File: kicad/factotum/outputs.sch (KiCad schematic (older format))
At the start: 68 parts

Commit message: working on schematic
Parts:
- removed R? (x14): R_Small, symbol Device:R_Small
- added C29, C30: 100n, symbol Device:C_Small
- added J13: Conn_01x10_Female, symbol Connector:Conn_01x10_Female
- added J18: Conn_01x10_Male, symbol Connector:Conn_01x10_Male
- added J19: Conn_01x18_Female, symbol Connector:Conn_01x18_Female
- added J20: Conn_01x18_Male, symbol Connector:Conn_01x18_Male
- added R51: 10k, symbol Device:R_Small
- added R54, R56, R58, R60, R62, R64, R66: 68, symbol Device:R_Small
- added R55, R57, R59, R61, R63, R65, R67: 56, symbol Device:R_Small
- added unit 5 of U6
- added unit 5 of U7
- D10, D11, D4, D5, D6, D7, D8, D9: renamed from D?; value LED_Dual_CAC -> SSL-LX3059IGW-CA
- R52: renamed from R?; value R_Small -> 68
- R53: renamed from R?; value R_Small -> 56
- gave numbers to parts that had none: 38
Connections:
- net DAC0 is gone; now on net DAC1: U10.3 (VOUTA)
- net +3.3VA: now also C29.1, U6.11 (V-), U7.11 (V-)
- net +3V3: now also C30.1, J19.1 (Pin_1), J20.1 (Pin_1), R51.2
- net DAC1: no longer U10.4 (VOUTB)
- net DAC2: now also U10.4 (VOUTB); no longer U10.5 (VOUTC)
- net DAC3: now also U10.5 (VOUTC); no longer U10.6 (VOUTD)
- net DAC4: now also U10.6 (VOUTD); no longer U10.14 (VOUTE)
- net DAC5: now also U10.14 (VOUTE); no longer U10.13 (VOUTF)
- net DAC6: now also U10.13 (VOUTF); no longer U10.12 (VOUTG)
- net DAC7: now also U10.12 (VOUTG); no longer U10.11 (VOUTH)
- net DAC8: now also U10.11 (VOUTH)
- net GND: now also C29.2, C30.2, J13.10 (Pin_10), J18.10 (Pin_10), J19.18 (Pin_18), J20.18 (Pin_18), U6.4 (V+), U7.4 (V+)
- net VREF: now also U6.10 (+), U6.12 (+), U6.5 (+), U7.10 (+), U7.12 (+), U7.5 (+), J13.1 (Pin_1), J18.1 (Pin_1); no longer U6.3 (+), U6.3 (+), U6.3 (+), U7.3 (+), U7.3 (+), U7.3 (+)
- net B_2: now reaches R43.1, R48.1
- net B_2: now also J18.3 (Pin_3); no longer J14.S
- net B_1: now reaches R31.1, R35.1
- net B_1: now also J18.2 (Pin_2); no longer J9.S
- net at R49.2: now also U7.7; no longer U7.1
- net at R40.1, R44.2: now also U7.6 (-); no longer U7.2 (-)
- net B_4: now reaches R44.1, R49.1
- net B_4: now also J18.5 (Pin_5); no longer J15.S
- net at R36.2: now also U6.7; no longer U6.1
- net at R26.1, R32.2: now also U6.6 (-); no longer U6.2 (-)
- net B_3: now reaches R32.1, R36.1
- net B_3: now also J18.4 (Pin_4); no longer J10.S
- net at R50.2: now also U7.8; no longer U7.1
- net at R41.1, R45.2: now also U7.9 (-); no longer U7.2 (-)
- net B_6: now reaches R45.1, R50.1
- net B_6: now also J18.7 (Pin_7); no longer J16.S
- net at R37.2: now also U6.8; no longer U6.1
- net at R27.1, R33.2: now also U6.9 (-); no longer U6.2 (-)
- net B_5: now reaches R33.1, R37.1
- net B_5: now also J18.6 (Pin_6); no longer J11.S
- net at R47.2: now also U7.14; no longer U7.1
- net at R42.1, R46.2: now also U7.13 (-); no longer U7.2 (-)
- net B_8: now reaches R46.1, R47.1
- net B_8: now also J18.9 (Pin_9); no longer J17.S
- net at R38.2: now also U6.14; no longer U6.1
- net at R28.1, R34.2: now also U6.13 (-); no longer U6.2 (-)
- net B_7: now reaches R34.1, R38.1
- net B_7: now also J18.8 (Pin_8); no longer J12.S
- net at U15.10 (LED4): now also J19.6 (Pin_6)
- net at U15.11 (LED5): now also J19.7 (Pin_7)
- net at U15.12 (LED6): now also J19.8 (Pin_8)
- net at U15.13 (LED7): now also J19.9 (Pin_9)
- net at U15.15 (LED8): now also J19.10 (Pin_10)
- net at U15.16 (LED9): now also J19.11 (Pin_11)
- net at U15.17 (LED10): now also J19.12 (Pin_12)
- net at U15.18 (LED11): now also J19.13 (Pin_13)
- net at U15.19 (LED12): now also J19.14 (Pin_14)
- net at U15.20 (LED13): now also J19.15 (Pin_15)
- net at U15.21 (LED14): now also J19.16 (Pin_16)
- net at U15.22 (LED15): now also J19.17 (Pin_17)
- net at U15.23 (~OE): now also R51.1
- net at U15.6 (LED0): now also J19.2 (Pin_2); no longer R52.2
- net at U15.7 (LED1): now also J19.3 (Pin_3); no longer R53.2
- net at U15.8 (LED2): now also J19.4 (Pin_4)
- net at U15.9 (LED3): now also J19.5 (Pin_5)
- net at D5.1 (K1): now also R55.1
- net at D5.3 (K2): now also R54.1
- net at D6.1 (K1): now also R57.1
- net at D6.3 (K2): now also R56.1
- net at D7.1 (K1): now also R59.1
- net at D7.3 (K2): now also R58.1
- net at D8.1 (K1): now also R61.1
- net at D8.3 (K2): now also R60.1
- net at D9.1 (K1): now also R63.1
- net at D9.3 (K2): now also R62.1
- net at D10.1 (K1): now also R65.1
- net at D10.3 (K2): now also R64.1
- net at D11.1 (K1): now also R67.1
- net at D11.3 (K2): now also R66.1
- net DAC_CS renamed DAC_SYNC
- net SPI1_MISO renamed SPI2_MISO
- net SPI1_MOSI renamed SPI2_MOSI
- net SPI1_SCLK renamed SPI2_SCLK
- new net G1_T: J20.3 (Pin_3), R53.2
- new net G2_T: J20.5 (Pin_5), R55.2
- new net G3_T: J20.7 (Pin_7), R57.2
- new net G4_T: J20.9 (Pin_9), R59.2
- new net G5_T: J20.11 (Pin_11), R61.2
- new net G6_T: J20.13 (Pin_13), R63.2
- new net G7_T: J20.15 (Pin_15), R65.2
- new net G8_T: J20.17 (Pin_17), R67.2
- new net R1_T: J20.2 (Pin_2), R52.2
- new net R2_T: J20.4 (Pin_4), R54.2
- new net R3_T: J20.6 (Pin_6), R56.2
- new net R4_T: J20.8 (Pin_8), R58.2
- new net R5_T: J20.10 (Pin_10), R60.2
- new net R6_T: J20.12 (Pin_12), R62.2
- new net R7_T: J20.14 (Pin_14), R64.2
- new net R8_T: J20.16 (Pin_16), R66.2
- new net T_1: J13.2 (Pin_2), J9.S
- new net T_2: J13.3 (Pin_3), J14.S
- new net T_3: J10.S, J13.4 (Pin_4)
- new net T_4: J13.5 (Pin_5), J15.S
- new net T_5: J11.S, J13.6 (Pin_6)
- new net T_6: J13.7 (Pin_7), J16.S
- new net T_7: J12.S, J13.8 (Pin_8)
- new net T_8: J13.9 (Pin_9), J17.S
- no-connect marks 8 -> 9
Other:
- moved on the sheet: J14, J15, J16, J17, R25, R26, R27, R28, R31, R32, R33, R34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

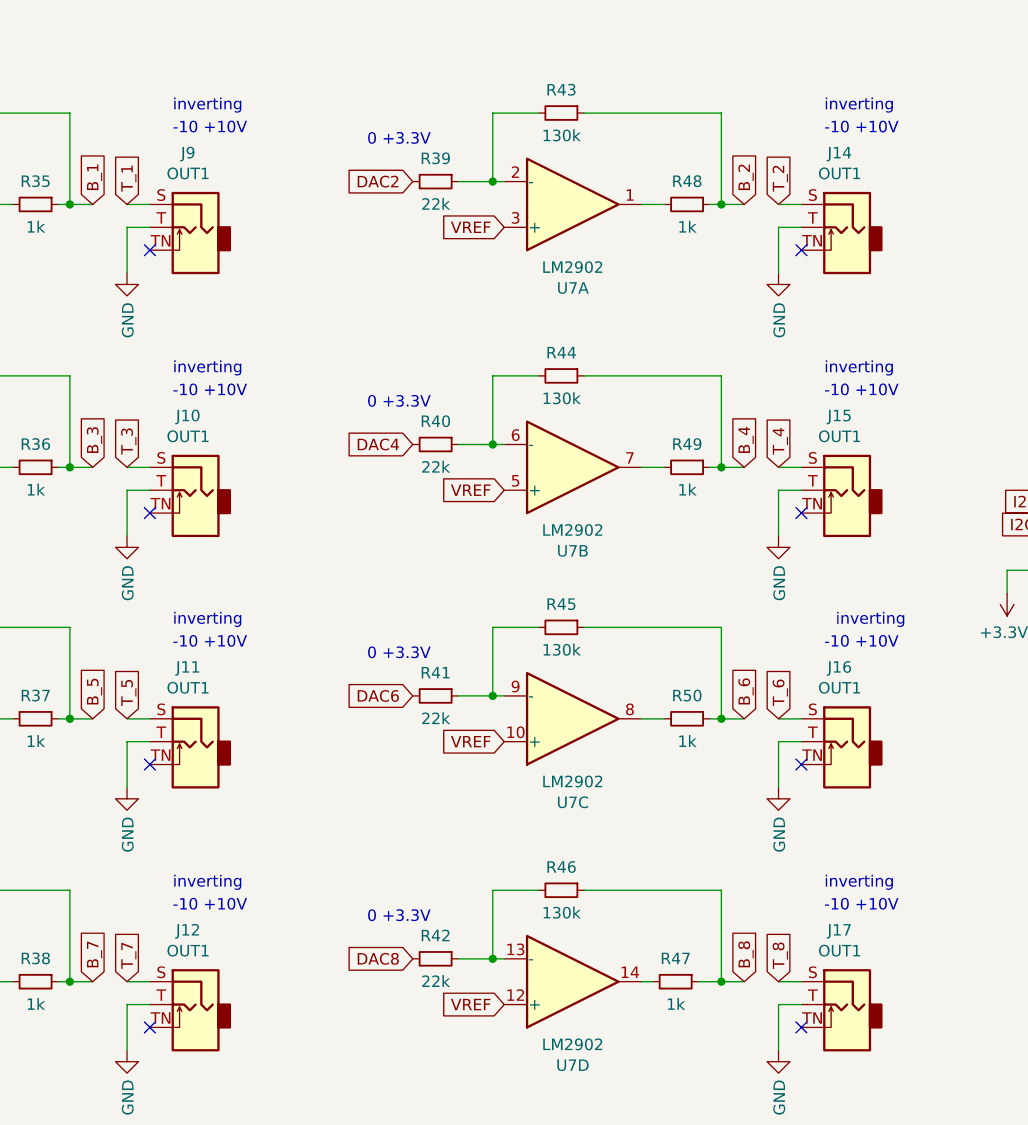
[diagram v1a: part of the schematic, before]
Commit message: initial layout of top board
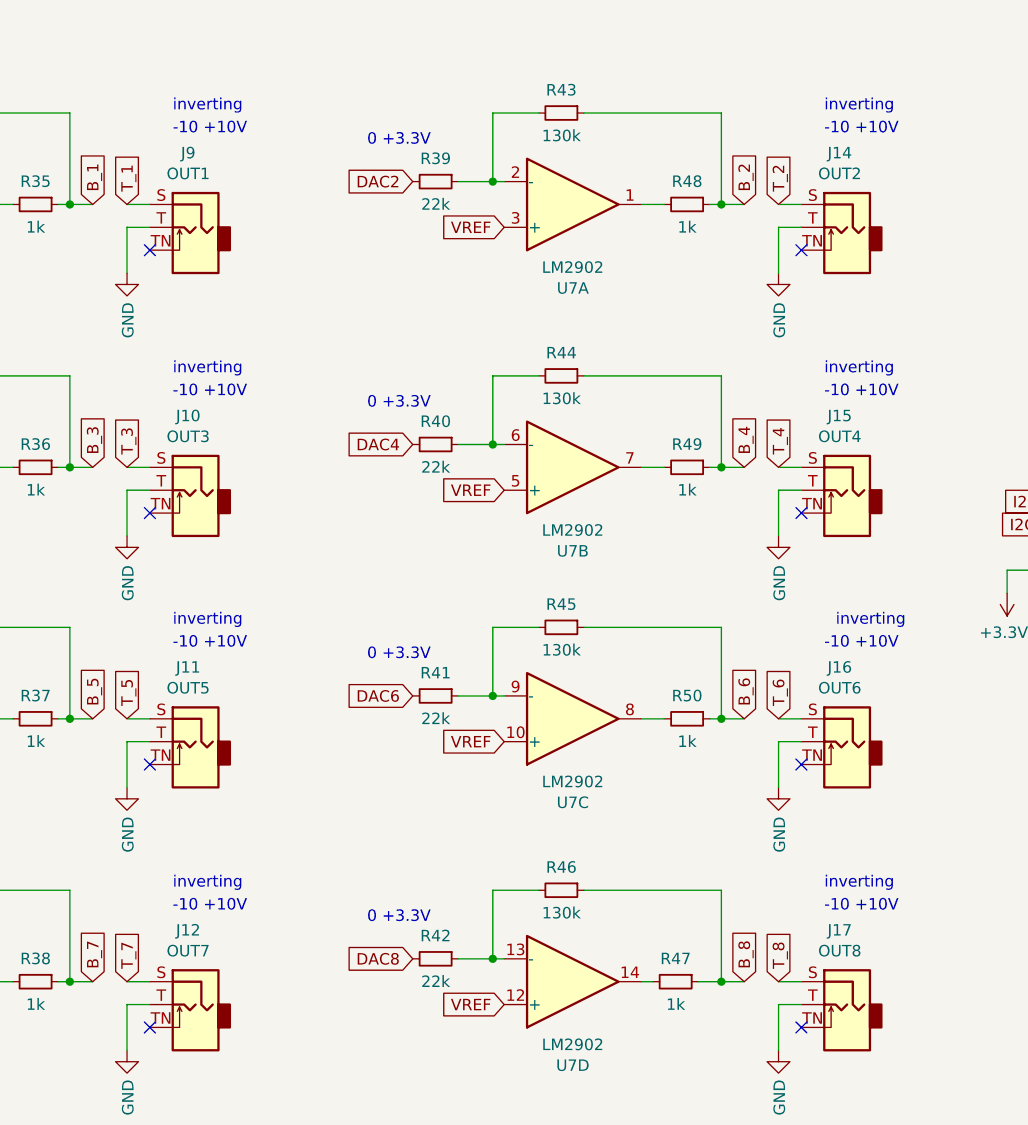
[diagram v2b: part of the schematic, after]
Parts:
- C29, C30: footprint (none) -> Capacitor_SMD:C_0603_1608Metric_Pad1.08x0.95mm_HandSolder
- D10, D11, D4, D5, D6, D7, D8, D9: footprint (none) -> LED_THT:LED_D3.0mm-3
- J10: value OUT1 -> OUT3; footprint (none) -> Connector_Audio:Jack_3.5mm_QingPu_WQP-PJ398SM_Vertical_CircularHoles
- J11: value OUT1 -> OUT5; footprint (none) -> Connector_Audio:Jack_3.5mm_QingPu_WQP-PJ398SM_Vertical_CircularHoles
- J12: value OUT1 -> OUT7; footprint (none) -> Connector_Audio:Jack_3.5mm_QingPu_WQP-PJ398SM_Vertical_CircularHoles
- J13: footprint (none) -> Connector_PinSocket_1.27mm:PinSocket_1x10_P1.27mm_Vertical
- J14: value OUT1 -> OUT2; footprint (none) -> Connector_Audio:Jack_3.5mm_QingPu_WQP-PJ398SM_Vertical_CircularHoles
- J15: value OUT1 -> OUT4; footprint (none) -> Connector_Audio:Jack_3.5mm_QingPu_WQP-PJ398SM_Vertical_CircularHoles
- J16: value OUT1 -> OUT6; footprint (none) -> Connector_Audio:Jack_3.5mm_QingPu_WQP-PJ398SM_Vertical_CircularHoles
- J17: value OUT1 -> OUT8; footprint (none) -> Connector_Audio:Jack_3.5mm_QingPu_WQP-PJ398SM_Vertical_CircularHoles
- J18: footprint (none) -> Connector_PinHeader_1.27mm:PinHeader_1x10_P1.27mm_Vertical
- J19: footprint (none) -> Connector_PinSocket_1.27mm:PinSocket_1x18_P1.27mm_Vertical
- J20: footprint (none) -> Connector_PinHeader_1.27mm:PinHeader_1x18_P1.27mm_Vertical
- J9: footprint (none) -> Connector_Audio:Jack_3.5mm_QingPu_WQP-PJ398SM_Vertical_CircularHoles
- R25, R26, R27, R28, R29, R30, R31, R32, R33, R34, R35, R36, R37, R38, R39, R40, R41, R42, R43, R44, R45, R46, R47, R48, R49, R50, R51, R52, R53, R54, R55, R56, R57, R58, R59, R60, R61, R62, R63, R64, R65, R66, R67: footprint (none) -> Resistor_SMD:R_0201_0603Metric_Pad0.64x0.40mm_HandSolder
- U10: footprint (none) -> Package_SO:TSSOP-16_4.4x5mm_P0.65mm
- U6, U7: footprint (none) -> Package_SO:TSSOP-14_4.4x5mm_P0.65mm
